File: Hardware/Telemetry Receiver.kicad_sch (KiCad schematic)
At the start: 30 parts, among them J2 USB_C_Receptacle_USB2.0, J3 S4B-XH-A-1, U1 LM1117-3.3, U2 USBLC6-2SC6, U3 STM32L4P5RET6, U5 36103205S, Y2 Crystal(32.756MHz)

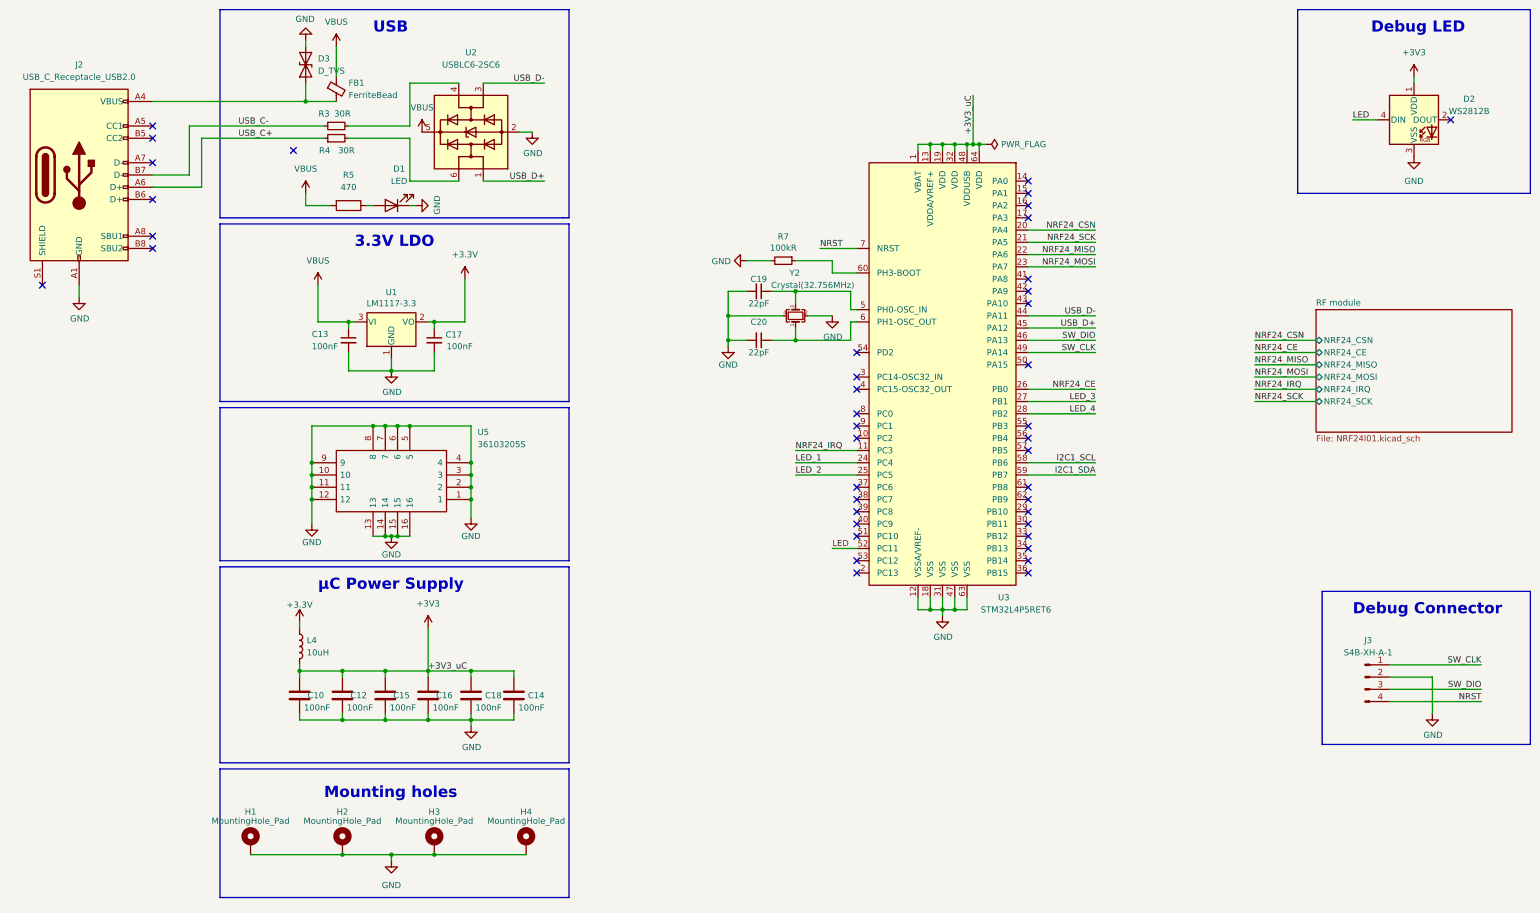
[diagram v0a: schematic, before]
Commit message: USB C changes
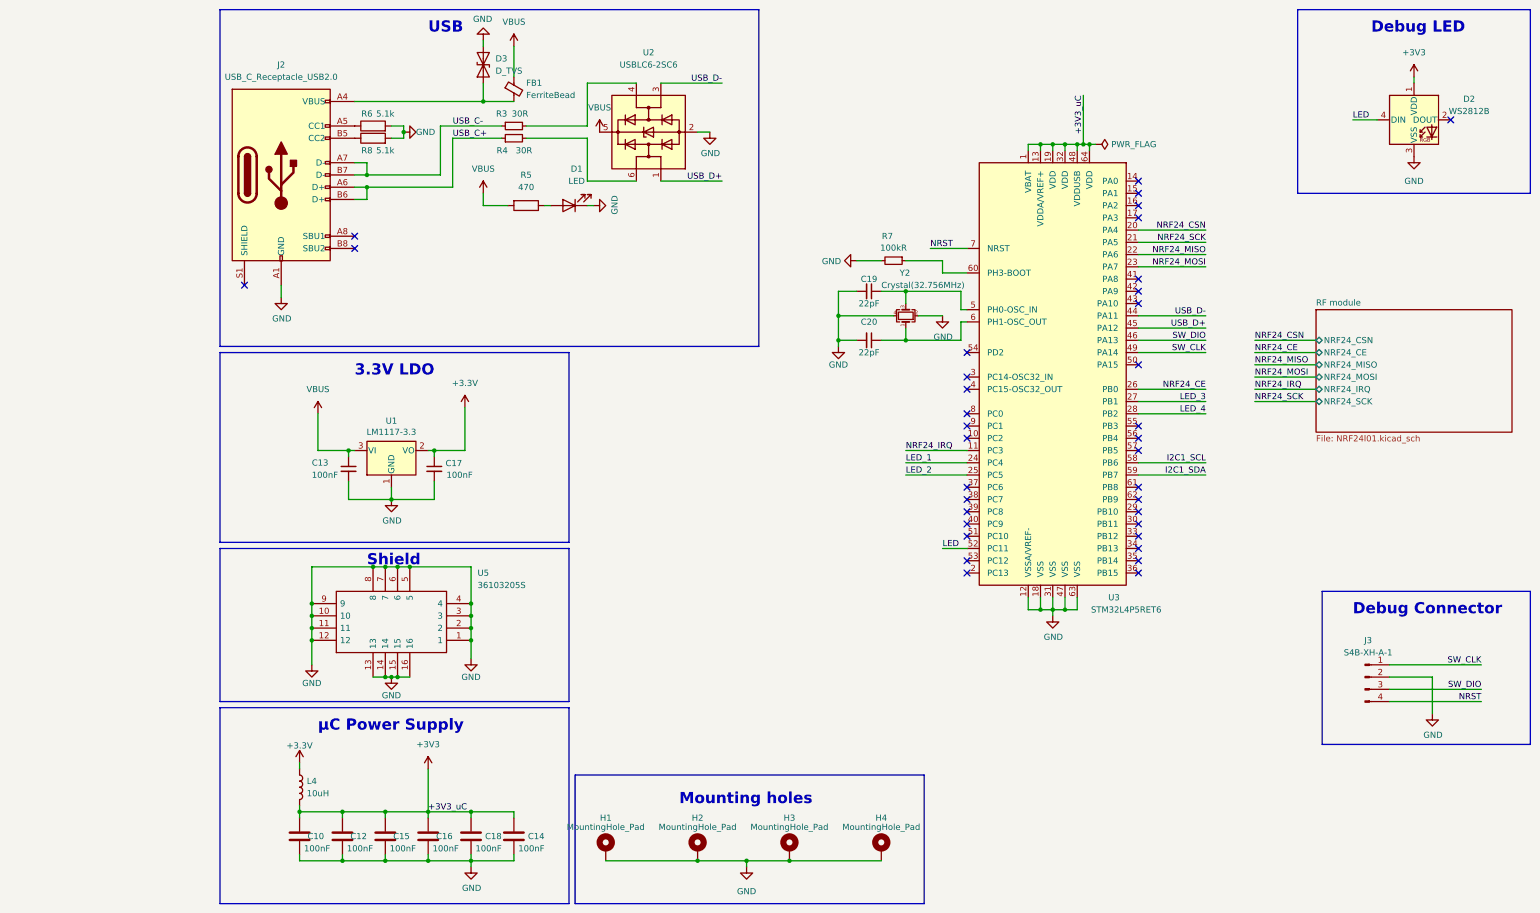
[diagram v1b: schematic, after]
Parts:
- added R6, R8: 5.1k, Resistor_SMD:R_0402_1005Metric, symbol Device:R
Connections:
- net GND: now also R6.2, R8.2
- net USB_C+: now also J2.B6 (D+)
- net USB_C-: now also J2.A7 (D-)
- net at J2.A5 (CC1): now also R6.1
- net at J2.B5 (CC2): now also R8.1
- no-connect marks 41 -> 36
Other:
- note added: "Shield"
- moved on the sheet: C10, C12, C13, C14, C15, C16, C17, C18, C19, C20, D1, D3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

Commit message: Changed footprint for available one
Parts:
- C19, C20: Manufacturer_Part_Number (none) -> CBR04C220J5GACAUTO; Mouser Part Number (none) -> 80-CBR04C220J5GAUTO; Mouser Price/Stock (none) -> 1,01 zł
- D3: Manufacturer_Part_Number (none) -> LXES02TAA1-144; Mouser Part Number (none) -> 81-LXES02TAA1-144; Mouser Price/Stock (none) -> 1,54 zł
- FB1: Manufacturer_Part_Number (none) -> BLM18HE152SH1D; Mouser Part Number (none) -> 81-BLM18HE152SH1D; Mouser Price/Stock (none) -> 1,30 zł
- J2: Manufacturer_Part_Number (none) -> USB4105-GF-A; Mouser Part Number (none) -> 640-USB4105-GF-A; Mouser Price/Stock (none) -> 3,90 zł
- L4: Manufacturer_Part_Number (none) -> LQW15DN100M00D; Mouser Part Number (none) -> 81-LQW15DN100M00D; Mouser Price/Stock (none) -> 9,86 zł
- R3, R4: Manufacturer_Part_Number (none) -> 0402WGJ0300TCE; Mouser Part Number (none) -> SMD0402-30R; Mouser Price/Stock (none) -> 0.04079
- R5: Manufacturer_Part_Number (none) -> RN73H1ETTP4700B25; Mouser Part Number (none) -> 660-RN73H1ETP4700B25; Mouser Price/Stock (none) -> 3,39 zł
- R6, R8: Manufacturer_Part_Number (none) -> RN73H1ETTP5101B25; Mouser Part Number (none) -> 660-RN73H1ETP5101B25; Mouser Price/Stock (none) -> 2,52 zł
- R7: Manufacturer_Part_Number (none) -> RN73H1ETTP1003B50; Mouser Part Number (none) -> 660-RN73H1ETP1003B50; Mouser Price/Stock (none) -> 2,91 zł
- U2: footprint Package_TO_SOT_SMD:SOT-666 -> Package_TO_SOT_SMD:SOT-23-6; Manufacturer_Part_Number (none) -> USBLC6-2SC6; Mouser Part Number (none) -> USBLC6-2SC6; Mouser Price/Stock (none) -> 1.076
- U5: Height 3.3 -> (none); Manufacturer_Name Wurth Elektronik -> (none); Manufacturer_Part_Number 36103205S -> 36103205S; Mouser Price/Stock https://www.mouser.co.uk/ProductDetail/Wurth-Elektronik/361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 -> 7,46 zł
- Y2: Manufacturer_Part_Number (none) -> FH3200025; Mouser Part Number (none) -> 729-FH3200025; Mouser Price/Stock (none) -> 5,96 zł
